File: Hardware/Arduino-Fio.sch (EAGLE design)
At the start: 65 parts, among them U1 MCP73831, U4 XBEE, U5 ATMEGA32U4, U6 MIC5219-3.3, X2 USB-MICROB, Y2 8MHz

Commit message: Midway hardware update
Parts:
- X2: value USB-MICROB -> USB_MICROB_PLUGCONN-11752; device SparkFun:USB-MICROB -> SparkFun-Connectors:USB_MICROB_PLUGCONN-11752
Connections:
- net USB_VCC: now also X2.VCC; no longer X2.VBUS
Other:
- moved on the sheet: R11, R12

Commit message: Fixing schematic frame
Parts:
- added U$2: REVISION, SparkFun-Aesthetics:REVISION
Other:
- note added: "N. Seidle"
- note added: "T. Klopfenstein"
- note removed: "Original design (LilyPad Arduino v1.6) by L. Buechley and N. Seidle"
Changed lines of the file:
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@@
 <?xml version="1.0" encoding="utf-8"?>
 <!DOCTYPE eagle SYSTEM "eagle.dtd">
-<eagle version="6.4">
+<eagle version="6.5.0">
 <drawing>
 <settings>
@@
 <part name="FRAME2" library="SparkFun-Aesthetics" deviceset="FRAME-LETTER" device=""/>
 <part name="LOGO1" library="SparkFun-Aesthetics" deviceset="OSHW-LOGO" device="L"/>
+<part name="U$2" library="SparkFun-Aesthetics" deviceset="REVISION" device=""/>
 </parts>
 <sheets>
 <sheet>
 <plain>
-<text x="172.72" y="10.16" size="3.175" layer="94" font="vector">Shigeru Kobayashi</text>
-<text x="149.86" y="5.08" size="1.6764" layer="95">Original design (LilyPad Arduino v1.6) by
- L. Buechley and N. Seidle</text>
+<text x="165.862" y="11.176" size="3.175" layer="94" font="vector">Shigeru Kobayashi</text>
 <text x="256.54" y="177.8" size="1.778" layer="97">Change to ATmega32U4</text>
 <text x="256.54" y="175.26" size="1.778" layer="97">Switch to microUSB</text>
@@
 <text x="254" y="147.32" size="1.778" layer="97">New on v31:</text>
 <text x="238.76" y="7.62" size="2.54" layer="97">v31</text>
+<text x="148.082" y="6.096" size="3.175" layer="94" font="vector">N. Seidle</text>
+<text x="194.564" y="6.35" size="3.175" layer="94" font="vector">T. Klopfenstein</text>
 </plain>
 <instances>
@@
 <instance part="JP5" gate="G$1" x="246.38" y="30.48"/>
 <instance part="LOGO1" gate="G$1" x="236.22" y="48.26"/>
+<instance part="U$2" gate="G$1" x="174.498" y="6.096"/>
 </instances>
 <busses>
@@
 </schematic>
 </drawing>
-<compatibility>
-<note version="6.3" minversion="6.2.2" severity="warning">
-Since Version 6.2.2 text objects can contain more than one line,
-which will not be processed correctly with this version.
-</note>
-</compatibility>
 </eagle>

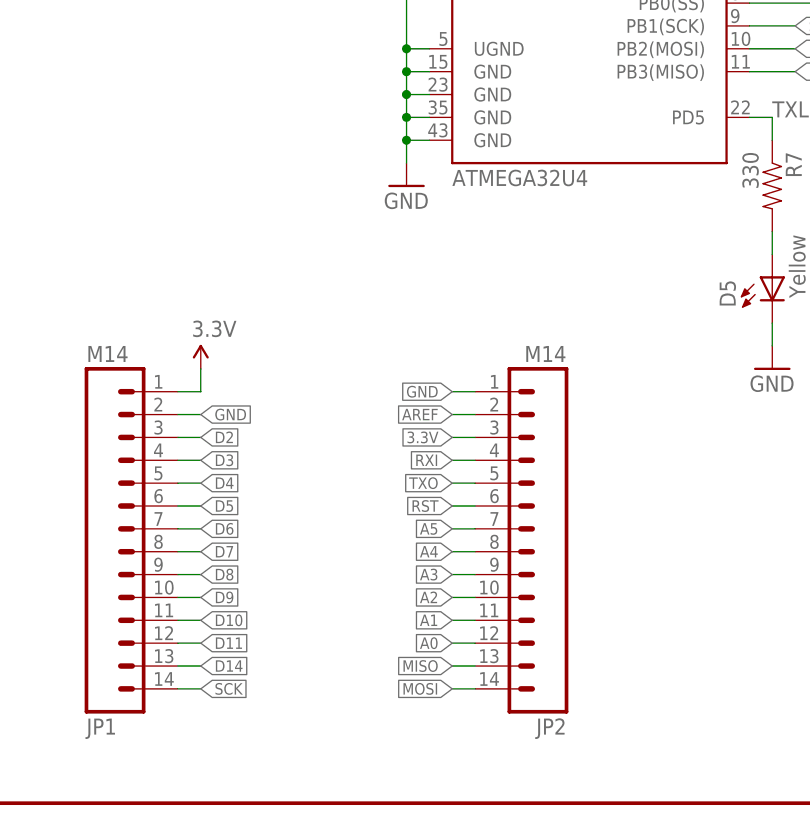
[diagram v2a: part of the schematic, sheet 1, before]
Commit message: Update Labeling
Updated individual board's silkscreen to correct pins to match the connection to the ATmega32U4 and Arduino core files:

* D17 | RxLED | SS
* D14 | MISO

Replace schematic package to match silkscreen from Brent's fix => [ https://github.com/sparkfun/SparkFun-Eagle-Libraries/issues/77#issuecomment-89820839 ]. Update the net for D17 to match silkscreen.

This should not affect the overall functionality of the board. =P
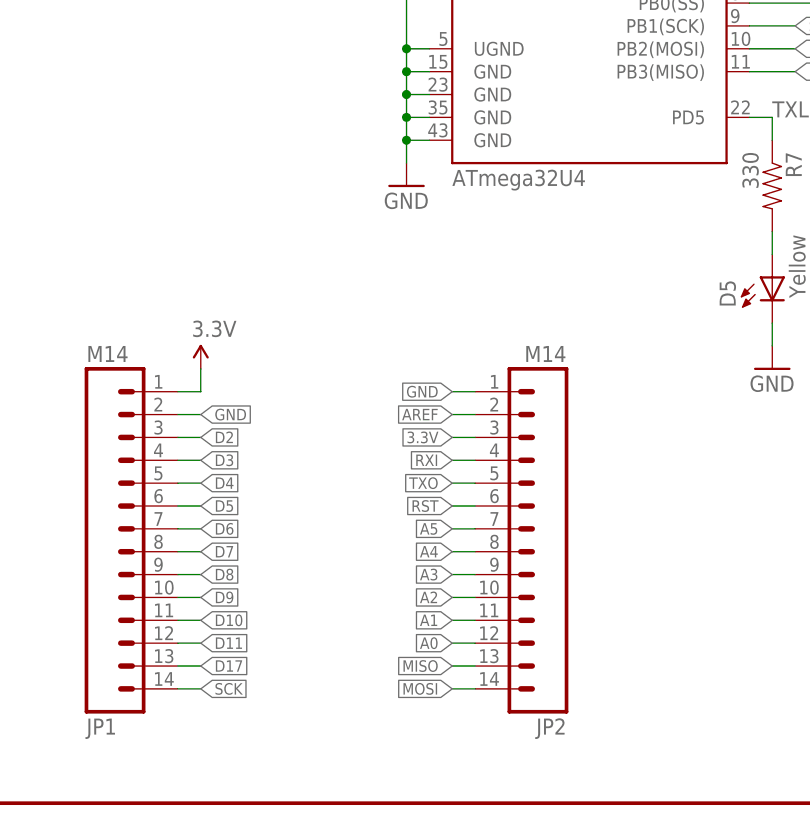
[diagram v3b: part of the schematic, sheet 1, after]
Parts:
- U5: value ATMEGA32U4 -> ATmega32U4; device Testing:ATMEGA32U41:1 -> SparkFun-IC-Microcontroller:ATMEGA32U41:1
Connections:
- net D14 renamed D17
